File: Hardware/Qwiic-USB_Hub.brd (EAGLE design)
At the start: 43.2 x 81.3 mm, 89 parts, among them J1 USB_A_FEMALE, J2 Qwiic Right Angle, J3 PTH, J4 Qwiic Right Angle, J6 USB_A_FEMALE, J8 USB_A_FEMALE, J9 USB_A_FEMALE, Q1 4.3A/20V/54mΩ, Q2 4.3A/20V/54mΩ, Q3 4.3A/20V/54mΩ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

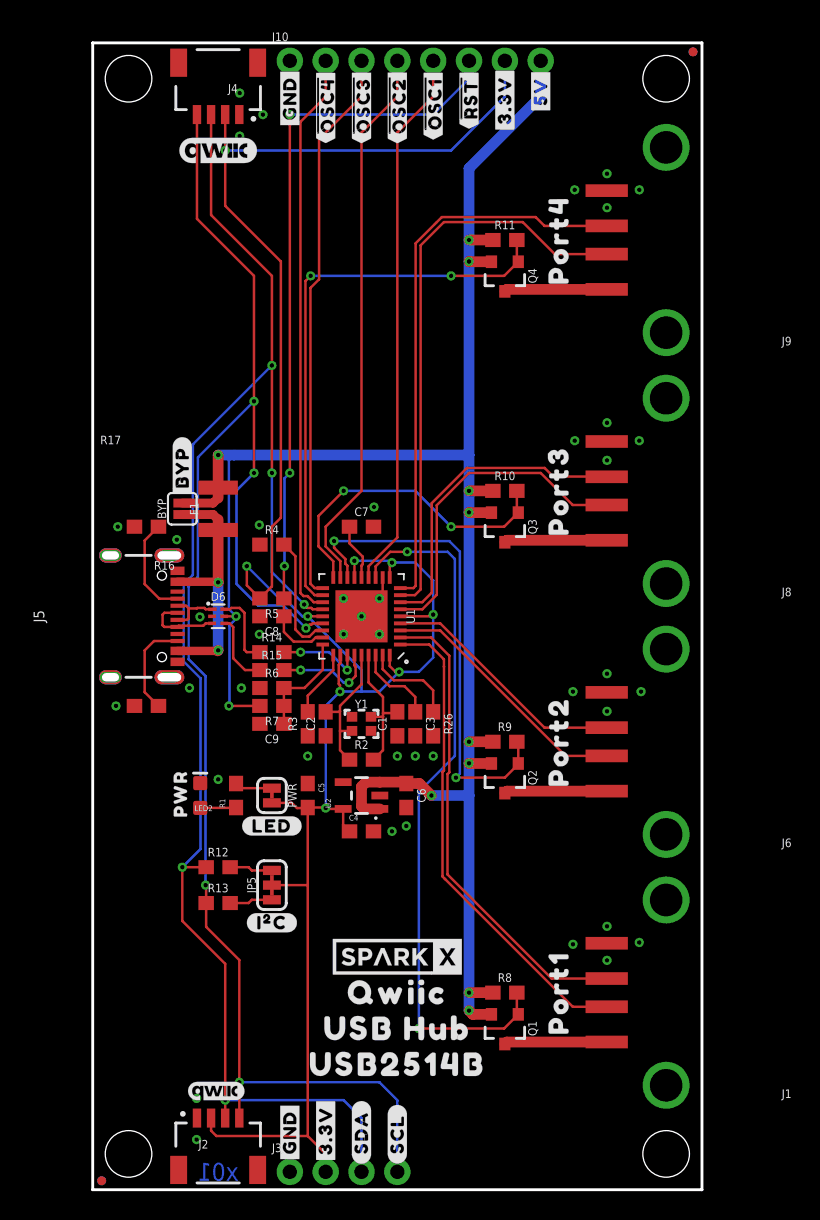
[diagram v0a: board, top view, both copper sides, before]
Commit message: Add ignore. Increase 3.3V width.
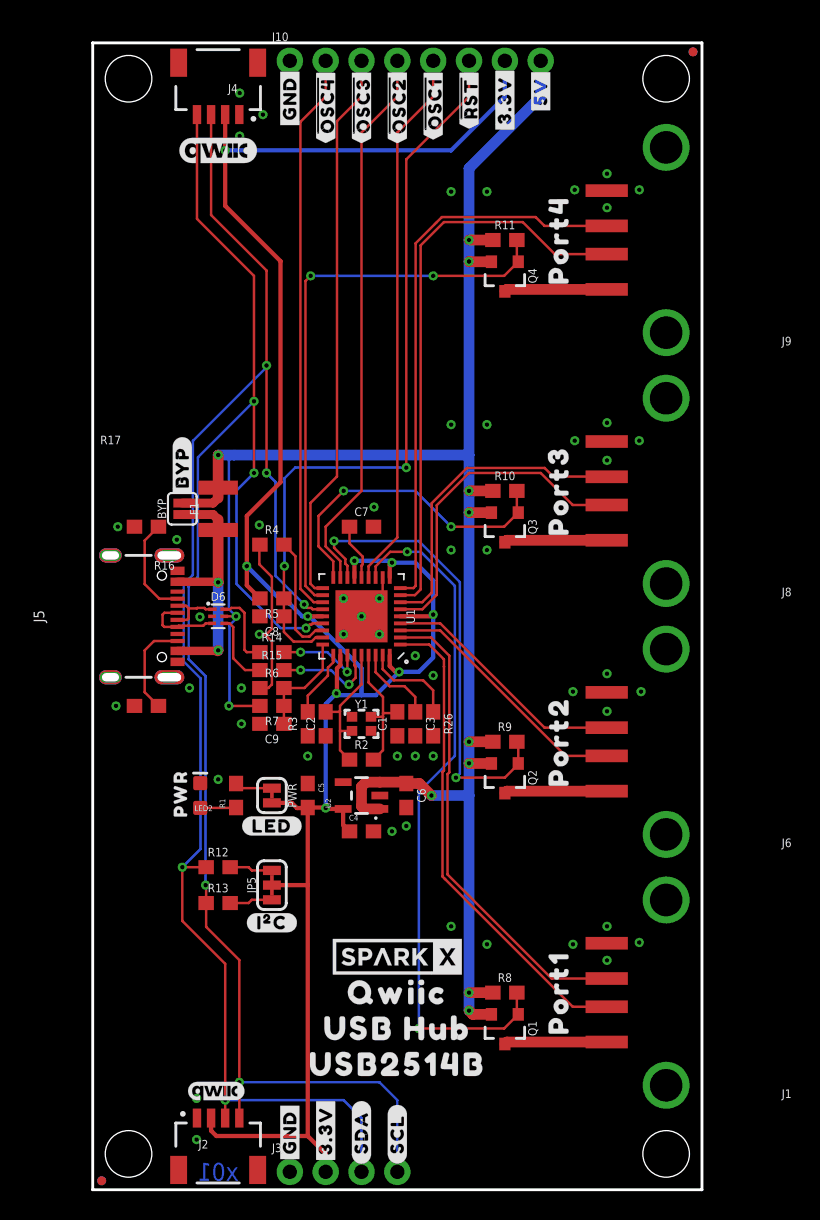
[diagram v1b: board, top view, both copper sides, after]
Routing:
- net GND: track 1.87 -> 14.4 mm, vias 42 -> 53
- net !RESET: track 55.0 -> 53.7 mm, vias 3 -> 2
- net PRTPWR2: track 34.8 -> 33.5 mm
- net 3.3V: track 157.7 -> 156.4 mm
- net PRTPWR1: track 50.4 -> 49.3 mm

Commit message: Add labels to bottom layer.
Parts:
- added U$11: (no value), output:#GND#5
- added U$24: (no value), output:##OSC4##1
- added U$25: (no value), output:##OSC3##0
- added U$28: (no value), output:##OSC2##2
- added U$29: (no value), output:##OSC1##3
- added U$31: (no value), output:##RST##4
- added U$32: (no value), output:#3#3V#6
- added U$37: (no value), output:#5V#7
- added U$38: SPARKX-LOGO4, SparkX:SPARKX-MEDIUM
- added U$39: (no value), output:QWIIC2
- added U$40: (no value), output:USB_HUB1
- added U$41: (no value), output:USB2514B0
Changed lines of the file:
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@@
 </element>
 <element name="U$23" library="output" package="#LED#0" value="" x="12.7" y="25.781" smashed="yes"/>
+<element name="U$11" library="output" package="#GND#5" value="" x="13.97" y="77.343" smashed="yes" rot="MR90"/>
+<element name="U$24" library="output" package="##OSC4##1" value="" x="16.51" y="76.835" smashed="yes" rot="MR90"/>
+<element name="U$25" library="output" package="##OSC3##0" value="" x="19.05" y="76.835" smashed="yes" rot="MR90"/>
+<element name="U$28" library="output" package="##OSC2##2" value="" x="21.59" y="76.835" smashed="yes" rot="MR90"/>
+<element name="U$29" library="output" package="##OSC1##3" value="" x="24.13" y="76.962" smashed="yes" rot="MR90"/>
+<element name="U$31" library="output" package="##RST##4" value="" x="26.67" y="77.343" smashed="yes" rot="MR90"/>
+<element name="U$32" library="output" package="#3#3V#6" value="" x="29.21" y="77.216" smashed="yes" rot="MR90"/>
+<element name="U$37" library="output" package="#5V#7" value="" x="31.75" y="77.851" smashed="yes" rot="MR90"/>
+<element name="U$38" library="SparkX" package="SPARKX-MEDIUM" value="SPARKX-LOGO4" x="21.59" y="16.51" smashed="yes" rot="MR0"/>
+<element name="U$39" library="output" package="QWIIC2" value="" x="21.59" y="13.97" smashed="yes" rot="MR0"/>
+<element name="U$40" library="output" package="USB_HUB1" value="" x="21.59" y="11.43" smashed="yes" rot="MR0"/>
+<element name="U$41" library="output" package="USB2514B0" value="" x="21.59" y="8.89" smashed="yes" rot="MR0"/>
 </elements>
 <signals>
